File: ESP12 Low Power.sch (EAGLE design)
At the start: 48 parts, among them Q1 FDN338P, U2 AP2112K-3.3TRG1

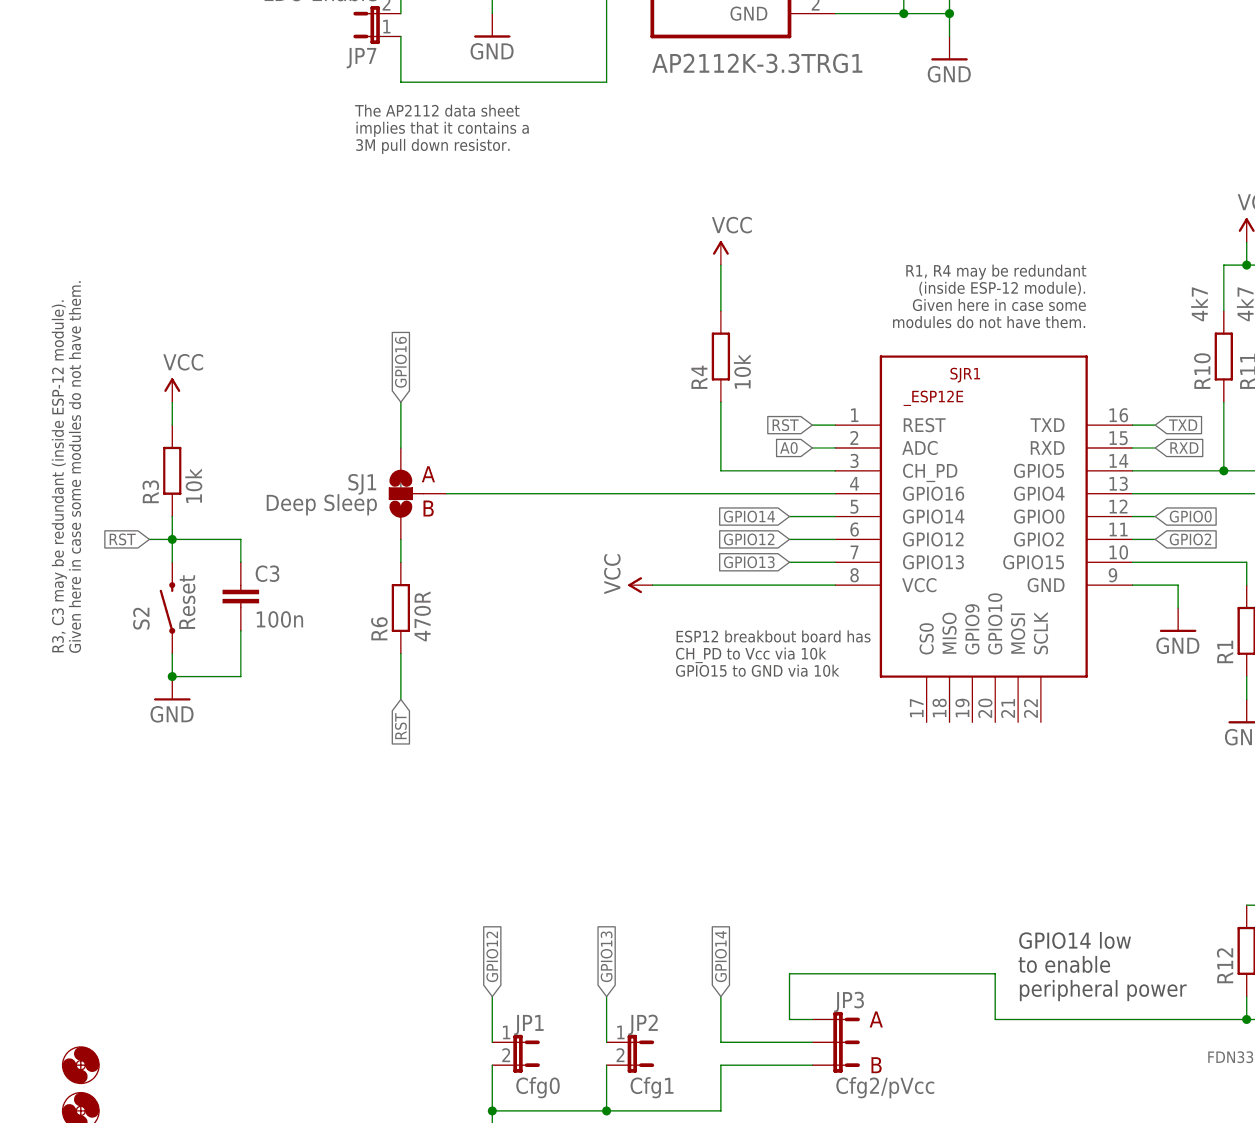
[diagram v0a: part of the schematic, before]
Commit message: Fixes and clarifications to README + some changes to schematic annotations (no circuit change)
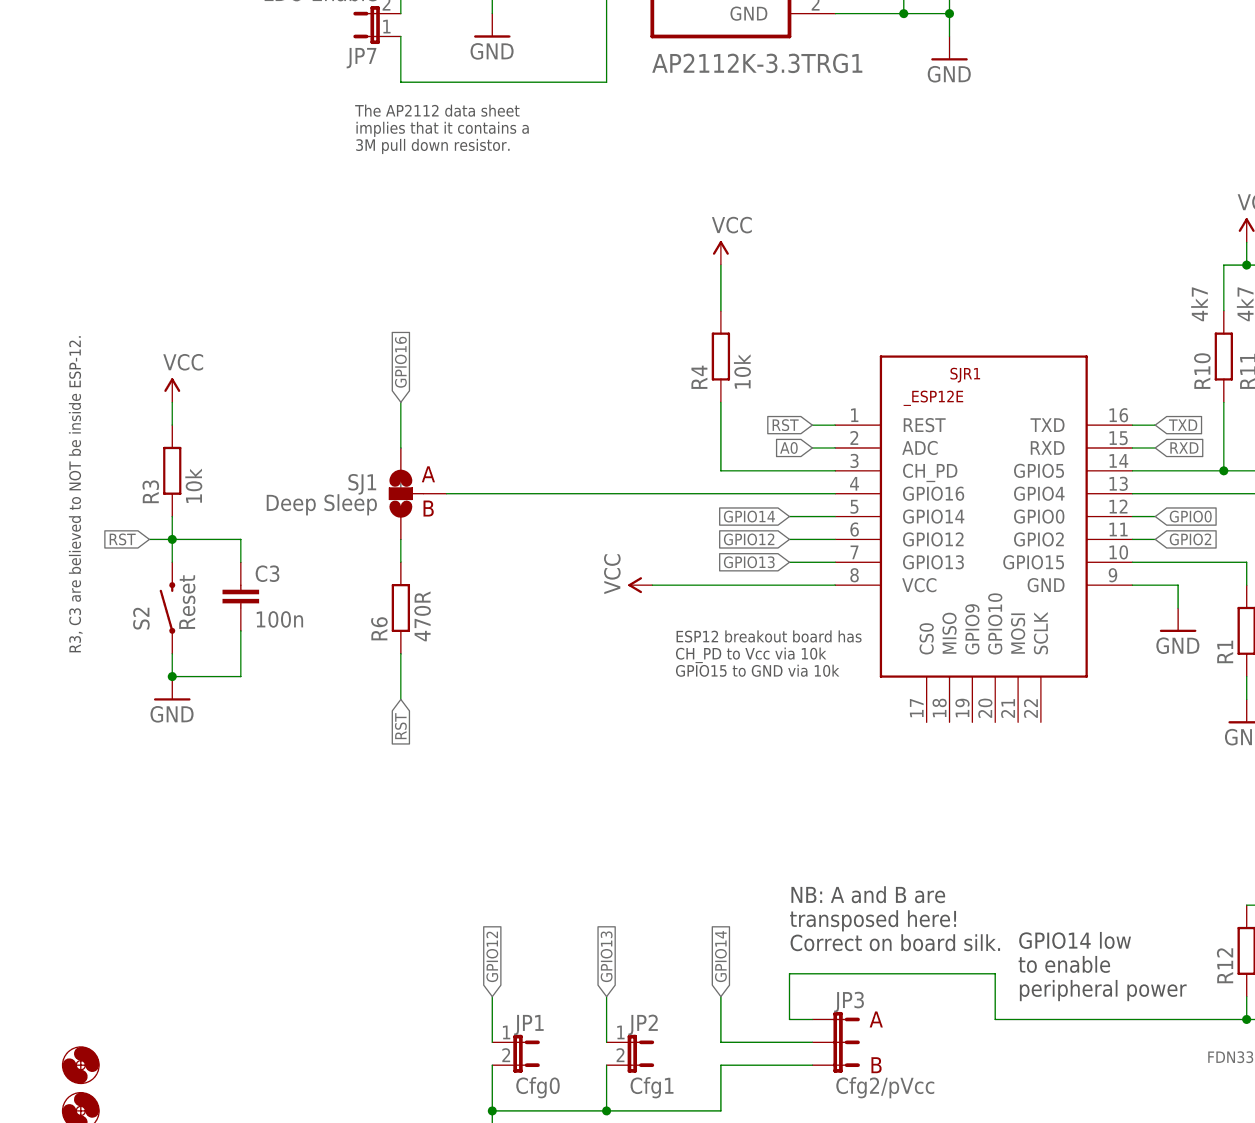
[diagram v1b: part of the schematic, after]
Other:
- note added: "ESP12 breakout board has CH_PD to Vcc via 10k GPIO15 to GND via 10k"
- note added: "NB: A and B are transposed here! Correct on board silk."
- note added: "R3, C3 are believed to NOT be inside ESP-12."
- note removed: "ESP12 breakbout board has CH_PD to Vcc via 10k GPIO15 to GND via 10k"
- note removed: "R1, R4 may be redundant (inside ESP-12 module). Given here in case some modules do not have them."
- note removed: "R3, C3 may be redundant (inside ESP-12 module). Given here in case some modules do not have them."
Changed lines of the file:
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@@
 <sheet>
 <plain>
-<text x="-165.1" y="48.26" size="1.27" layer="97" rot="R90">R3, C3 may be redundant (inside ESP-12 module).
-Given here in case some modules do not have them.</text>
+<text x="-165.1" y="48.26" size="1.27" layer="97" rot="R90">R3, C3 are believed to NOT be inside ESP-12.</text>
 <text x="-10.16" y="55.88" size="1.27" layer="97">R9, LED1:
 As on NodeMCU &amp; ESP12
@@
 if the code is checking
 Vcc.</text>
-<text x="-99.06" y="45.72" size="1.27" layer="97">ESP12 breakbout board has
+<text x="-99.06" y="45.72" size="1.27" layer="97">ESP12 breakout board has
 CH_PD to Vcc via 10k
 GPIO15 to GND via 10k</text>
@@
 to LED V drop and
 current.</text>
-<text x="-53.34" y="91.44" size="1.27" layer="97" rot="R180">R1, R4 may be redundant
-(inside ESP-12 module).
-Given here in case some
-modules do not have them.</text>
 <text x="-60.96" y="10.16" size="1.778" layer="97">GPIO14 low
 to enable
@@
 <text x="78.74" y="40.64" size="1.27" layer="97" rot="R270">NB: different
 power pins</text>
+<text x="-86.36" y="15.24" size="1.778" layer="97">NB: A and B are
+transposed here!
+Correct on board silk.</text>
 </plain>
 <instances>

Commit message: Changes for v1.1 See Github issues
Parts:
- added EP3: (no value), Master 2016:USB-FCI_SMD***
- added S3: Cfg1 Reed, Master 2016:SWITCH-MOMENTARY-2PTH_REED
- added S4: Rst Reed, Master 2016:SWITCH-MOMENTARY-2PTH_REED
- added SJ4, SJ5: SOLDERJUMPERTRACE, Master 2016:SOLDERJUMPERTRACE
- added SW1: SWITCH_SPDTMULTICOMP_MS2, Master 2016:SWITCH_SPDTMULTICOMP_MS2
- renumbered SL1 to EP1, SL2 to EP2
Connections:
- new net V_REG: C2.+, EP2-2.S, SW1.S, U2.VOUT
- net GND: now also EP3.GND, S3.1, S4.1
- net GPIO13: now also S3.2
- net N$13: now also EP3.VBUS
- net N$3: now also SJ4.1
- net N$8: now also SJ4.2
- net RST: now also S4.2
- net VCC: now also SJ5.2, SW1.P; no longer C2.+, EP2-2.S, U2.VOUT
- net VCC@P: now also SJ5.1
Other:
- note added: "Device substitutions: for LDO, AP2112K-3.3, use MIC5504-3.3 for RTS Reset, 1N5711, use BAT48"
- moved on the sheet: JP1, U$1
